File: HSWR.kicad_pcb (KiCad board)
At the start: 4 copper layers, 152 x 139 mm, 159 parts, among them IC1 B1212S-2W, IC3 JW5052C, IC4 ADM3054, IC5 ADuM4160, J1 USB_B, J2 IO, J3 B+, J4 B-, J5 U, J6 V, J7 W, J8 SWD, J9 AVR-ISP-6, Q1 IXFK300N20X3, Q2 IXFK300N20X3, Q3 IXFK300N20X3, Q4 IXFK300N20X3, Q5 IXFK300N20X3, Q6 IXFK300N20X3, Q7 Q_NMOS_GDS, U1 ACS781xLRTR-150B, U10 AM26LV32xD, U11 ADuM120N1, U12 ADuM120N1, U13 PC355, U2 ACS781xLRTR-150B, U3 ACS781xLRTR-150B, U4 STM32F405RGTx, U5 IRS2186, U6 IRS2186, U7 IRS2186, U8 AP1117-50, U9 ATtiny13A-SU, Y1 8MHz

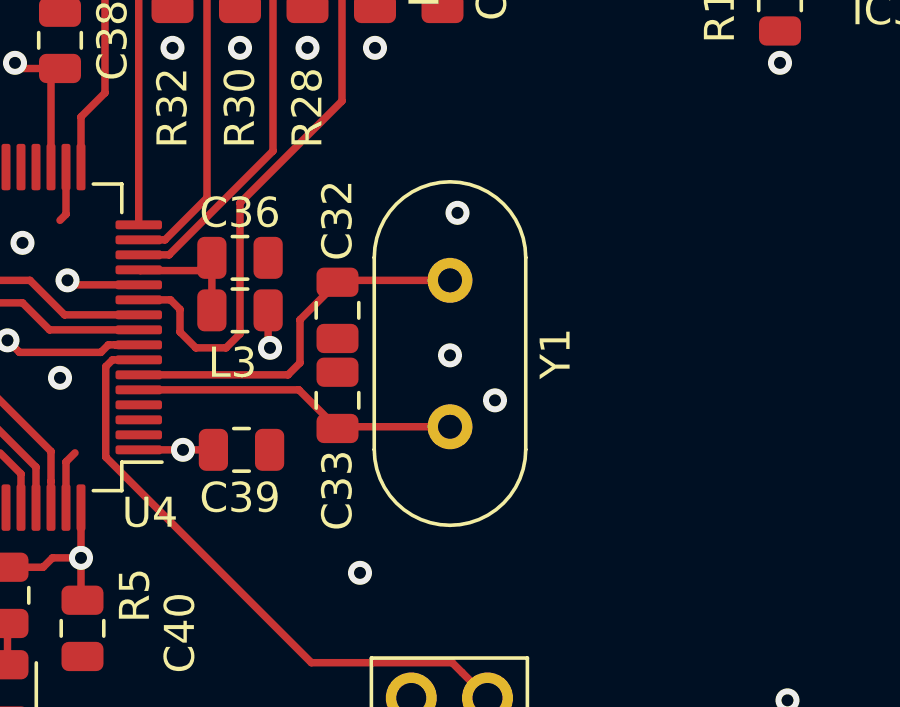
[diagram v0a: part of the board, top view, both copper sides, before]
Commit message: - upgraded project to KiCAD 7 - cleaned project - changed hall pullups to 10k
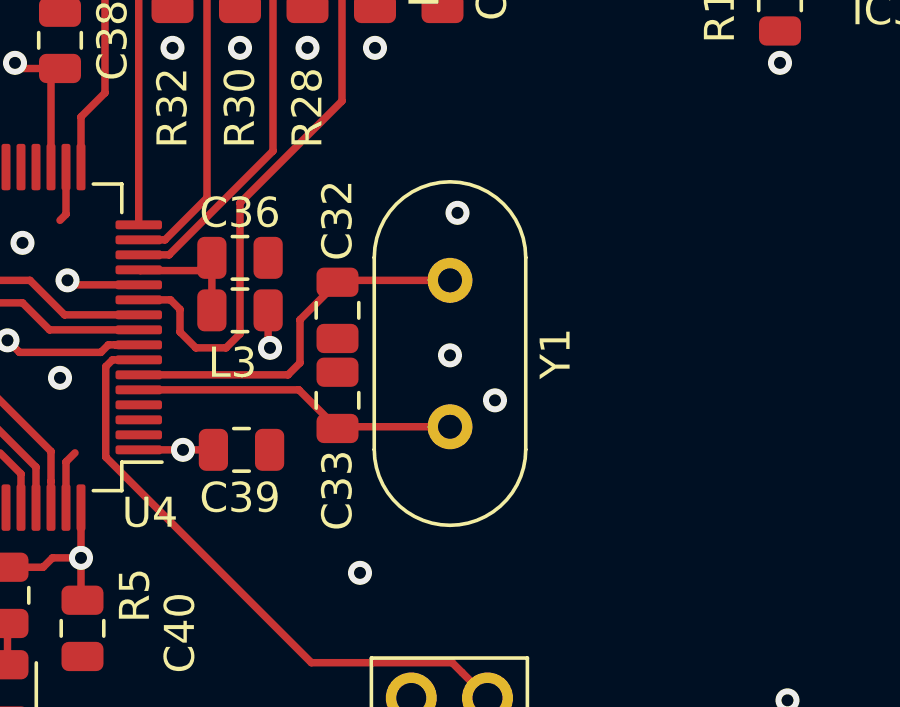
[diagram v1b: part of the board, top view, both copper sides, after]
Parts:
- R18, R19, R21, R22, R24, R25: value 1R -> 4R7
- R38, R39, R47: value 1k -> 10k
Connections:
- net /MCU/CAN_VSS_SENSE renamed /CAN bus transceiver/V+Sense
- net /USB/Device_D+ renamed /MCU/USB_DP
- net /USB/Device_D- renamed /MCU/USB_DM
- net /iso IO/UART renamed /MCU/UART_RX
- IC4 pad 10: (no net) -> unconnected-(IC4-VREF-Pad10)
- J8 pad 6: (no net) -> unconnected-(J8-Pin_6-Pad6)
- U1 pad 4: (no net) -> unconnected-(U1-NC-Pad4)
- U1 pad 7: (no net) -> unconnected-(U1-NC-Pad7)
- U10 pad 4: (no net) -> unconnected-(U10-G-Pad4)
- U2 pad 4: (no net) -> unconnected-(U2-NC-Pad4)
- U2 pad 7: (no net) -> unconnected-(U2-NC-Pad7)
- U3 pad 4: (no net) -> unconnected-(U3-NC-Pad4)
- U3 pad 7: (no net) -> unconnected-(U3-NC-Pad7)
- U4 pad 2: (no net) -> unconnected-(U4-PC13-Pad2)
- U4 pad 20: (no net) -> unconnected-(U4-PA4-Pad20)
- U4 pad 21: (no net) -> unconnected-(U4-PA5-Pad21)
- U4 pad 22: (no net) -> unconnected-(U4-PA6-Pad22)
- U4 pad 23: (no net) -> unconnected-(U4-PA7-Pad23)
- U4 pad 24: (no net) -> unconnected-(U4-PC4-Pad24)
- U4 pad 25: (no net) -> unconnected-(U4-PC5-Pad25)
- U4 pad 26: (no net) -> unconnected-(U4-PB0-Pad26)
- U4 pad 27: (no net) -> unconnected-(U4-PB1-Pad27)
- U4 pad 28: (no net) -> unconnected-(U4-PB2-Pad28)
- U4 pad 3: (no net) -> unconnected-(U4-PC14-Pad3)
- U4 pad 33: (no net) -> unconnected-(U4-PB12-Pad33)
- U4 pad 4: (no net) -> unconnected-(U4-PC15-Pad4)
- U4 pad 40: (no net) -> unconnected-(U4-PC9-Pad40)
- U4 pad 53: (no net) -> unconnected-(U4-PC12-Pad53)
- U4 pad 54: (no net) -> unconnected-(U4-PD2-Pad54)
- U4 pad 55: (no net) -> unconnected-(U4-PB3-Pad55)
- U4 pad 56: (no net) -> unconnected-(U4-PB4-Pad56)
- U4 pad 57: (no net) -> unconnected-(U4-PB5-Pad57)
- U4 pad 58: (no net) -> unconnected-(U4-PB6-Pad58)
- U4 pad 59: (no net) -> unconnected-(U4-PB7-Pad59)
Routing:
- added copper zone on In1.Cu, net +12VA
- added copper zone on In2.Cu, net +3V3
- added copper zone on In2.Cu, net +5VA
- added copper zone on In1.Cu, net /Mosfet driver/U_VP
- added copper zone on In2.Cu, net /Mosfet driver/U_VP
- added copper zone on In1.Cu, net /Mosfet driver/V_VP
- added copper zone on In2.Cu, net /Mosfet driver/V_VP
- added copper zone on In1.Cu, net /Mosfet driver/W_VP
- added copper zone on In2.Cu, net /Mosfet driver/W_VP
- added copper zone on In1.Cu, net GND
- removed copper zone on GND, net +12VA
- removed copper zone on Power1, net +3V3
- removed copper zone on Power1, net +5VA
- removed copper zone on GND, net /Mosfet driver/U_VP
- removed copper zone on Power1, net /Mosfet driver/U_VP
- removed copper zone on GND, net /Mosfet driver/V_VP
- removed copper zone on Power1, net /Mosfet driver/V_VP
- removed copper zone on GND, net /Mosfet driver/W_VP
- removed copper zone on Power1, net /Mosfet driver/W_VP
- removed copper zone on GND, net GND
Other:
- net class Default removed
- net class iso removed

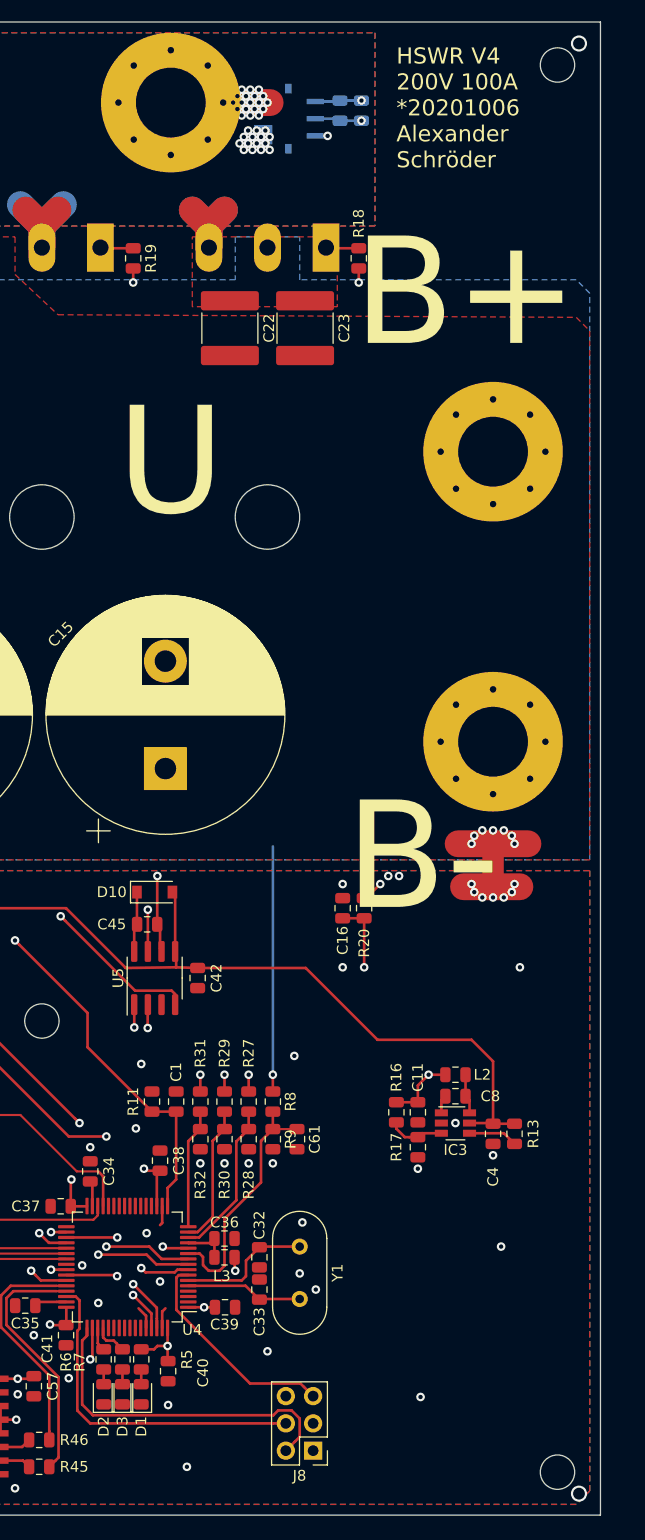
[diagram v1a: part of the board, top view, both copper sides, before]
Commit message: HSWR V4.1: - added opamp for better voltage measurement
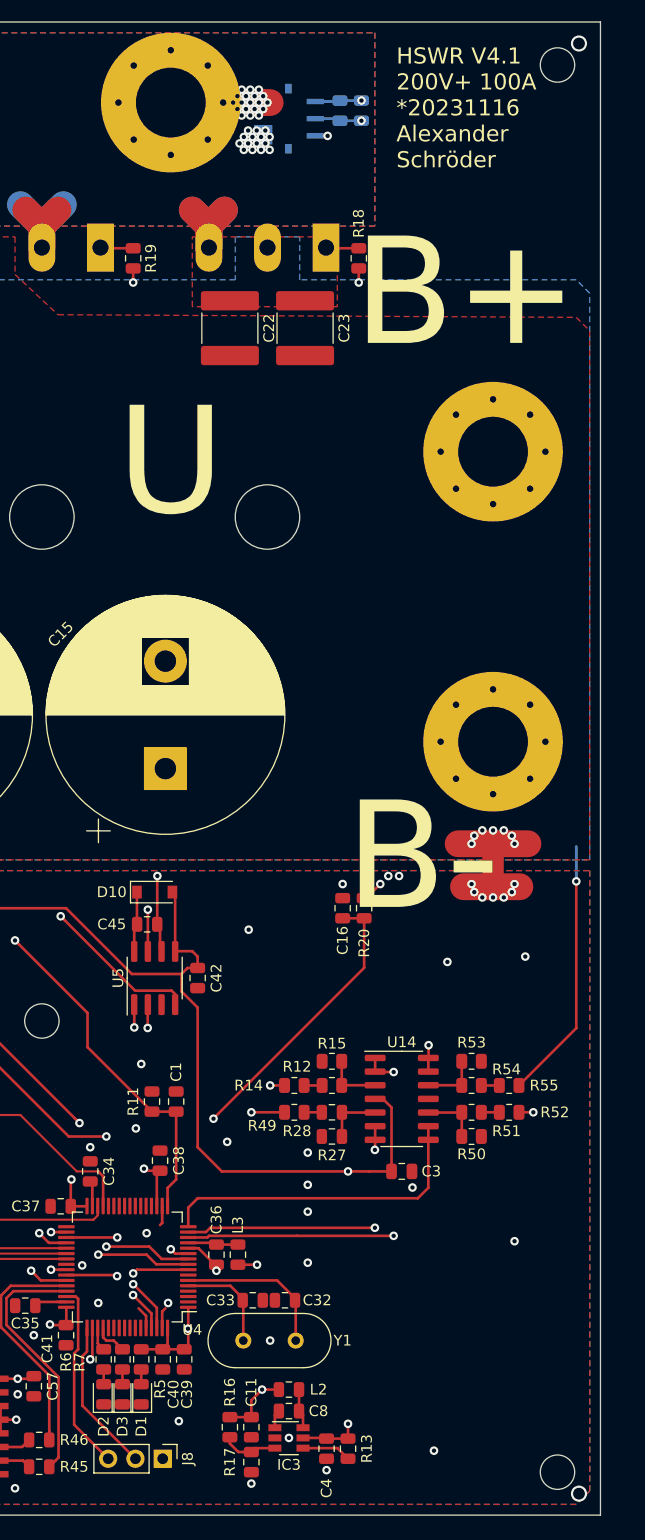
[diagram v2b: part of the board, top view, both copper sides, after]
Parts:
- removed C61: 1u, Capacitor_SMD:C_0805_2012Metric
- removed R29, R31, R8: 300k 0.1%, Resistor_SMD:R_0805_2012Metric
- removed R30, R32, R9: 4k7 0.1%, Resistor_SMD:R_0805_2012Metric
- added C3: 1u, Capacitor_SMD:C_0805_2012Metric, F.Cu at (200.5, 131.0)
- added R12: 150k, Resistor_SMD:R_0805_2012Metric, F.Cu at (194.0, 123.0)
- added R14: 150k, Resistor_SMD:R_0805_2012Metric, F.Cu at (190.5, 123.0)
- added R15: 4k7, Resistor_SMD:R_0805_2012Metric, F.Cu at (194.0, 120.8)
- added R49: 150k, Resistor_SMD:R_0805_2012Metric, F.Cu at (190.5, 125.5)
- added R50: 4k7, Resistor_SMD:R_0805_2012Metric, F.Cu at (207.0, 127.8)
- added R51: 150k, Resistor_SMD:R_0805_2012Metric, F.Cu at (207.0, 125.5)
- added R52: 150k, Resistor_SMD:R_0805_2012Metric, F.Cu at (210.5, 125.5)
- added R53: 4k7, Resistor_SMD:R_0805_2012Metric, F.Cu at (207.0, 120.8)
- added R54: 150k, Resistor_SMD:R_0805_2012Metric, F.Cu at (207.0, 123.0)
- added R55: 150k, Resistor_SMD:R_0805_2012Metric, F.Cu at (210.5, 123.0)
- added U14: Opamp_Quad, Package_SO:SO-14_3.9x8.65mm_P1.27mm, F.Cu at (200.5, 124.2)
- J8: value SWD -> ISP; footprint Connector_PinHeader_2.54mm:PinHeader_2x03_P2.54mm_Vertical -> Connector_PinHeader_2.54mm:PinHeader_1x03_P2.54mm_Vertical
- R27: value 300k 0.1% -> 4k7
- R28: value 4k7 0.1% -> 150k
- moved C11 33.2 mm to (186.5, 154.8)
- moved C4 33.2 mm to (193.5, 156.8)
- moved C8 33.2 mm to (190.0, 153.3)
- moved IC3 33.2 mm to (190.0, 155.8)
- moved L2 33.2 mm to (190.0, 151.3)
- moved R13 33.2 mm to (195.5, 156.8)
- moved R16 33.2 mm to (184.5, 154.8)
- moved R17 33.2 mm to (186.5, 158.1)
- moved J8 14.0 mm to (178.2, 157.8), turned to -90 degrees
- moved Y1 8.76 mm to (190.6, 146.8), turned to 180 degrees
- moved R27 8.40 mm to (194.0, 127.8), turned to 0 degrees
- moved R28 8.14 mm to (194.0, 125.5), turned to 180 degrees
- moved C39 6.16 mm to (180.2, 148.5), turned to -90 degrees
- moved C32 4.65 mm to (189.6, 143.0), turned to 0 degrees
- moved C36 1.68 mm to (183.2, 138.8), turned to 90 degrees
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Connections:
- J8 pad 1: +3V3 -> GND
- J8 pad 3: GND -> SWDIO
- R27 pad 1: /Mosfet driver/U_VP -> GND
- R27 pad 2: /MCU/U_U -> Net-(U14B-+)
- R28 pad 1: /MCU/U_U -> Net-(U14B-+)
- R28 pad 2: GND -> Net-(R28-Pad2)
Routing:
- net /Mosfet driver/W_VP: track 191.6 -> 236.2 mm
- net +12V: track 203.0 -> 236.7 mm, vias 1 -> 3
- net /MCU/U_U: track 14.6 -> 37.4 mm, vias 0 -> 2
- net NRST: track 20.3 -> 0.00 mm
- net /MCU/W_U: track 11.2 -> 30.6 mm
- net SWCLK: track 32.0 -> 14.4 mm
- net SWDIO: track 31.6 -> 17.6 mm
- net /MCU/V_U: track 13.1 -> 27.0 mm, vias 0 -> 2
- net /CAN bus transceiver/CAN_RX: track 68.9 -> 55.2 mm
- net /MCU/BUS_U: track 23.1 -> 36.1 mm, vias 0 -> 2
- net /Mosfet driver/V_VP: track 162.2 -> 168.3 mm
- net Net-(U14D-+): track 0.00 -> 5.37 mm
- net Net-(U14C-+): track 0.00 -> 5.37 mm
- net Net-(U14A-+): track 0.00 -> 5.37 mm
- net Net-(U14B-+): track 0.00 -> 5.18 mm
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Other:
- board text added: "HSWR V4.1 200V+ 100A *20231116 Alexander Schröder"
- board text removed: "HSWR V4 200V 100A *20201006 Alexander Schröder"

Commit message: - some layout work
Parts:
- removed the C29 at (110.8, 32.2)
- removed the C30 at (112.8, 32.2)
- removed the C31 at (114.8, 106.8)
- removed C51: 100n, Capacitor_SMD:C_0805_2012Metric
- removed JP1: H1, Jumper:SolderJumper-2_P1.3mm_Open_TrianglePad1.0x1.5mm
- removed JP3: H2, Jumper:SolderJumper-2_P1.3mm_Open_TrianglePad1.0x1.5mm
- removed JP4: H3, Jumper:SolderJumper-2_P1.3mm_Open_TrianglePad1.0x1.5mm
- removed JP5: EN, Jumper:SolderJumper-3_P2.0mm_Open_TrianglePad1.0x1.5mm
- removed NT1: Net-Tie_2, NetTie:NetTie-2_SMD_Pad2.0mm
- removed the R26 at (112.8, 106.8)
- removed the R38 at (103.8, 137.0)
- removed the R39 at (101.5, 138.2)
- removed the R47 at (103.8, 130.0)
- removed the U3 at (106.0, 33.0)
- added C10: 100n, Capacitor_SMD:C_0805_2012Metric, F.Cu at (183.0, 235.1)
- added C13: 10n, Capacitor_SMD:C_0805_2012Metric, F.Cu at (45.5, 108.5)
- added C60: 1u, Capacitor_SMD:C_0805_2012Metric, F.Cu at (174.5, 197.6)
- added C61: 1u, Capacitor_SMD:C_0805_2012Metric, F.Cu at (174.5, 200.7)
- added C62: 1u, Capacitor_SMD:C_0805_2012Metric, F.Cu at (174.5, 203.7)
- added C63: 1u, Capacitor_SMD:C_0805_2012Metric, F.Cu at (174.5, 206.7)
- added C64: 1u, Capacitor_SMD:C_0805_2012Metric, F.Cu at (174.5, 209.7)
- added C65: 1u, Capacitor_SMD:C_0805_2012Metric, F.Cu at (174.5, 212.7)
- added C66: 1u, Capacitor_SMD:C_0805_2012Metric, F.Cu at (174.5, 215.7)
- added C67: 100n, Capacitor_SMD:C_0805_2012Metric, F.Cu at (48.8, 240.4)
- added C68: 1u, Capacitor_SMD:C_0805_2012Metric, F.Cu at (48.8, 243.4)
- added C69: 330u 250V, Capacitor_THT:CP_Radial_D22.0mm_P10.00mm_SnapIn, F.Cu at (126.8, 163.5)
- added C70: 330u 250V, Capacitor_THT:CP_Radial_D22.0mm_P10.00mm_SnapIn, F.Cu at (103.2, 163.5)
- added C71: 4n7, Capacitor_SMD:C_0805_2012Metric, F.Cu at (48.8, 246.4)
- added C72: 330u 250V, Capacitor_THT:CP_Radial_D22.0mm_P10.00mm_SnapIn, F.Cu at (79.8, 163.5)
- added C73: 330u 250V, Capacitor_THT:CP_Radial_D22.0mm_P10.00mm_SnapIn, F.Cu at (56.2, 163.5)
- added C74: 330u 250V, Capacitor_THT:CP_Radial_D22.0mm_P10.00mm_SnapIn, F.Cu at (32.8, 163.5)
- added C75: 2u2 250V, Capacitor_SMD:C_2220_5750Metric, F.Cu at (34.8, 205.0)
- added C76: 2u2 250V, Capacitor_SMD:C_2220_5750Metric, F.Cu at (27.8, 205.0)
- added C77: 2u2 250V, Capacitor_SMD:C_2220_5750Metric, F.Cu at (70.0, 205.0)
- added C78: 2u2 250V, Capacitor_SMD:C_2220_5750Metric, F.Cu at (77.0, 205.0)
- added C79: 2u2 250V, Capacitor_SMD:C_2220_5750Metric, F.Cu at (111.8, 205.0)
- added C80: 2u2 250V, Capacitor_SMD:C_2220_5750Metric, F.Cu at (118.8, 205.0)
- added C81: 100n, Capacitor_SMD:C_0805_2012Metric, F.Cu at (53.3, 240.4)
- added C82: 1u, Capacitor_SMD:C_0805_2012Metric, F.Cu at (53.3, 243.4)
- added C83: 4n7, Capacitor_SMD:C_0805_2012Metric, F.Cu at (53.3, 246.4)
- added D10: RFN2L4S, Diode_SMD:D_SOD-123, F.Cu at (196.6, 213.4)
- added D8: RFN2L4S, Diode_SMD:D_SOD-123, F.Cu at (196.6, 206.7)
- added D9: RFN2L4S, Diode_SMD:D_SOD-123, F.Cu at (196.6, 210.0)
- added J10: W2, MountingHole:MountingHole_6.5mm_Pad_Via, F.Cu at (43.2, 225.5)
- added J13: CAN, Connector_Phoenix_MC:PhoenixContact_MCV_1,5_4-G-3.5_1x04_P3.50mm_Vertical, F.Cu at (19.0, 141.5)
- added J14: Motor1, Connector_Phoenix_MC:PhoenixContact_MCV_1,5_6-G-3.5_1x06_P3.50mm_Vertical, F.Cu at (19.0, 93.5)
- added J15: FAN, Connector_Phoenix_MC:PhoenixContact_MCV_1,5_2-G-3.5_1x02_P3.50mm_Vertical, F.Cu at (34.8, 115.2)
- added J8: U2, MountingHole:MountingHole_6.5mm_Pad_Via, F.Cu at (127.2, 225.5)
- added J9: V2, MountingHole:MountingHole_6.5mm_Pad_Via, F.Cu at (85.2, 225.5)
- added Q10: IXFK300N20X3, HSWR:TO-264-3_Horizontal_TabUp_6mm_hole, B.Cu at (68.0, 212.0)
- added Q11: IXFK300N20X3, HSWR:TO-264-3_Horizontal_TabUp_6mm_hole, B.Cu at (88.8, 212.0)
- added Q12: IXFK300N20X3, HSWR:TO-264-3_Horizontal_TabUp_6mm_hole, B.Cu at (25.8, 212.0)
- added Q13: IXFK300N20X3, HSWR:TO-264-3_Horizontal_TabUp_6mm_hole, B.Cu at (46.8, 212.0)
- added Q8: IXFK300N20X3, HSWR:TO-264-3_Horizontal_TabUp_6mm_hole, B.Cu at (109.8, 212.0)
- added Q9: IXFK300N20X3, HSWR:TO-264-3_Horizontal_TabUp_6mm_hole, B.Cu at (130.8, 212.0)
- added R18: 100R, Resistor_SMD:R_0805_2012Metric, F.Cu at (41.5, 108.5)
- added R19: 1k, Resistor_SMD:R_0805_2012Metric, F.Cu at (43.5, 108.5)
- added R20: 10k, Resistor_SMD:R_0805_2012Metric, F.Cu at (39.5, 108.5)
- added R50: 4k7, Resistor_SMD:R_0805_2012Metric, F.Cu at (187.4, 197.6)
- added R51: 4k7, Resistor_SMD:R_0805_2012Metric, F.Cu at (187.4, 200.6)
- added R52: 4k7, Resistor_SMD:R_0805_2012Metric, F.Cu at (187.4, 203.5)
- added R53: 150k, Resistor_SMD:R_0805_2012Metric, F.Cu at (191.8, 197.6)
- added R54: 150k, Resistor_SMD:R_0805_2012Metric, F.Cu at (191.8, 200.6)
- added R55: 150k, Resistor_SMD:R_0805_2012Metric, F.Cu at (191.8, 203.5)
- added R56: 150k, Resistor_SMD:R_0805_2012Metric, F.Cu at (196.2, 197.6)
- added R57: 150k, Resistor_SMD:R_0805_2012Metric, F.Cu at (196.2, 200.6)
- added R58: 150k, Resistor_SMD:R_0805_2012Metric, F.Cu at (196.2, 203.5)
- added R59: 4R7, Resistor_SMD:R_0805_2012Metric, F.Cu at (106.8, 211.2)
- added R60: 4R7, Resistor_SMD:R_0805_2012Metric, F.Cu at (127.8, 211.2)
- added R61: 1k, Resistor_SMD:R_0805_2012Metric, F.Cu at (62.2, 246.2)
- added R62: 4R7, Resistor_SMD:R_0805_2012Metric, F.Cu at (65.0, 211.2)
- added R63: 4R7, Resistor_SMD:R_0805_2012Metric, F.Cu at (85.8, 211.2)
- added R64: 1k, Resistor_SMD:R_0805_2012Metric, F.Cu at (66.6, 246.2)
- added R65: 4R7, Resistor_SMD:R_0805_2012Metric, F.Cu at (22.8, 211.2)
- added R66: 4R7, Resistor_SMD:R_0805_2012Metric, F.Cu at (43.8, 211.2)
- added RN1: 10k, Resistor_SMD:R_Array_Convex_4x0603, F.Cu at (29.0, 119.8)
- added RN2: 10k, Resistor_SMD:R_Array_Convex_4x0603, F.Cu at (26.5, 127.8)
- added U15: IRS2186, Package_SO:SOIC-8_3.9x4.9mm_P1.27mm, F.Cu at (181.2, 187.0)
- added U16: IRS2186, Package_SO:SOIC-8_3.9x4.9mm_P1.27mm, F.Cu at (181.0, 205.8)
- added U17: IRS2186, Package_SO:SOIC-8_3.9x4.9mm_P1.27mm, F.Cu at (181.0, 212.3)
- added U18: Opamp_Quad, Package_SO:SO-14_3.9x8.65mm_P1.27mm, F.Cu at (189.4, 210.1)
- added U19: ACS781xLRTR-150B, Sensor_Current:Allegro_PSOF-7_4.8x6.4mm_P1.60mm, F.Cu at (34.7, 246.6)
- added U20: ACS781xLRTR-150B, Sensor_Current:Allegro_PSOF-7_4.8x6.4mm_P1.60mm, F.Cu at (34.7, 254.6)
- added U5: ADuM120N, Package_SO:SOIC-8_3.9x4.9mm_P1.27mm, F.Cu at (48.0, 116.0)
- added U6: ADuM261N, Package_SO:SOIC-16W_7.5x12.8mm_P1.27mm, F.Cu at (48.0, 126.2)
- C41: renamed from C20; footprint Capacitor_SMD:C_2220_5650Metric -> Capacitor_SMD:C_2220_5750Metric
- C42: renamed from C21; footprint Capacitor_SMD:C_2220_5650Metric -> Capacitor_SMD:C_2220_5750Metric
- C43: renamed from C22; footprint Capacitor_SMD:C_2220_5650Metric -> Capacitor_SMD:C_2220_5750Metric
- C44: renamed from C23; footprint Capacitor_SMD:C_2220_5650Metric -> Capacitor_SMD:C_2220_5750Metric
- C45: renamed from C24; footprint Capacitor_SMD:C_2220_5650Metric -> Capacitor_SMD:C_2220_5750Metric
- C46: renamed from C25; footprint Capacitor_SMD:C_2220_5650Metric -> Capacitor_SMD:C_2220_5750Metric
- C49: value 100n -> 4n7
- C59: value 100n -> 22u/6V3
- J1: renamed from J2; value IO -> Motor1; footprint Connector_IDC:IDC-Header_2x08_P2.54mm_Vertical_Lock -> Connector_Phoenix_MC:PhoenixContact_MCV_1,5_6-G-3.5_1x06_P3.50mm_Vertical
- J5: value U -> U1
- J6: value V -> V1
- J7: value W -> W1
- R3: value 120R -> 470R
- R33, R34, R4: value 120R -> 150k
- R37: value 100R -> 150k
- U10: value AM26LV32xD -> IRS2186; footprint Package_SO:SOIC-16_3.9x9.9mm_P1.27mm -> Package_SO:SOIC-8_3.9x4.9mm_P1.27mm
- U11: value ADuM120N1 -> IRS2186
- U12: value ADuM120N1 -> ACS781xLRTR-150B; footprint Package_SO:SOIC-8_3.9x4.9mm_P1.27mm -> Sensor_Current:Allegro_PSOF-7_4.8x6.4mm_P1.60mm; moved to B.Cu
- U13: value PC355 -> ACS781xLRTR-150B; footprint Package_SO:SO-4_4.4x4.3mm_P2.54mm -> Sensor_Current:Allegro_PSOF-7_4.8x6.4mm_P1.60mm; moved to B.Cu
- U3: renamed from U9; footprint Package_SO:SOIJ-8_5.3x5.3mm_P1.27mm -> Package_SO:SO-8_5.3x6.2mm_P1.27mm
- moved U10 121.6 mm to (180.8, 223.3)
- moved U11 116.1 mm to (189.8, 223.8)
- moved U13 106.1 mm to (74.2, 224.0), turned to 0 degrees
- moved R3 102.1 mm to (178.8, 149.6)
- moved R33 102.1 mm to (178.8, 142.8)
- moved R34 102.1 mm to (178.8, 139.6)
- moved R4 102.1 mm to (178.8, 146.3)
- moved C49 101.8 mm to (95.5, 247.8)
- moved U12 92.7 mm to (116.5, 224.0)
- moved REF** 87.1 mm to (163.2, 229.0)
- moved REF** 87.1 mm to (19.2, 229.0)
- moved R27 69.8 mm to (35.8, 129.5)
- moved C6 69.2 mm to (34.8, 145.6)
- moved C12 68.1 mm to (41.5, 114.0), turned to 180 degrees
- moved Q1 67.3 mm to (29.2, 107.8), turned to 90 degrees
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- renumbered C60 to C11, C50 to C12, C58 to C14, C32 to C16, C33 to C17, C34 to C18, C35 to C19, C55 to C2, C36 to C20, C37 to C21, C38 to C22, C39 to C23, C40 to C24, C41 to C25, C42 to C26, C43 to C27, C44 to C28, C45 to C29, C56 to C3, C46 to C30, C47 to C31, C3 to C32, C12 to C33, C13 to C34, C14 to C35, C15 to C36, C16 to C37, C17 to C38, C18 to C39, C57 to C4, C19 to C40, C26 to C47, C27 to C48, C28 to C49, C52 to C5, C2 to C53, C4 to C54, C5 to C55, C6 to C56, C8 to C57, C9 to C58, C11 to C59, C53 to C6, C54 to C7, C62 to C8, C48 to C9, D4 to D1, D3 to D2, D2 to D3, D1 to D4, D10 to D5, D11 to D6, D12 to D7, IC5 to IC1, IC4 to IC2, IC1 to IC3, IC3 to IC4, J9 to J11, J8 to J12, J1 to J2, L3 to L1, Q7 to Q1, Q1 to Q2, Q2 to Q3, Q3 to Q4, Q4 to Q5, Q5 to Q6, Q6 to Q7, R7 to R1, R42 to R10, R43 to R11, R44 to R12, R45 to R13, R46 to R14, R40 to R15, R1 to R16, R2 to R17, R6 to R2, R35 to R22, R48 to R26, R36 to R27, R15 to R29, R5 to R3, R27 to R30, R50 to R31, R12 to R32, R28 to R33, R51 to R34, R14 to R35, R49 to R36, R52 to R37, R18 to R38, R19 to R39, R55 to R4, R20 to R40, R21 to R41, R22 to R42, R23 to R43, R24 to R44, R25 to R45, R13 to R47, R16 to R48, R17 to R49, R54 to R5, R53 to R6, R10 to R7, R11 to R8, R41 to R9, U14 to U1, U6 to U10, U7 to U11, U1 to U12, U2 to U13, U8 to U2, U4 to U8, U5 to U9
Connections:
- net /MCU/U_I renamed /MCU/U1_I
- net /MCU/U_PWM_H renamed /MCU/U1_PWM_H
- net /MCU/U_PWM_L renamed /MCU/U1_PWM_L
- net /MCU/U_U renamed /MCU/U1_U
- net /MCU/V_U renamed /MCU/V1_U
- net /MCU/W_U renamed /MCU/W1_U
- net /Mosfet driver/U_GH renamed /Mosfet driver 1/U_GH
- net /Mosfet driver/U_GL renamed /Mosfet driver 1/U_GL
- C29 pad 2: /Mosfet driver/U_VP -> /Mosfet driver 1/U_VP
- C30 pad 1: Net-(D11-K) -> Net-(D6-K)
- C30 pad 2: /Mosfet driver/V_VP -> /Mosfet driver 1/V_VP
- C31 pad 1: Net-(D12-K) -> Net-(D7-K)
- C31 pad 2: /Mosfet driver/W_VP -> /Mosfet driver 1/W_VP
- C49 pad 1: /MCU/V_I -> /Power MOSFETS 1/V_I
- C49 pad 1: +5VA -> /Power MOSFETS 1/V_I
- C49 pad 2: Earth -> GND
- C8 pad 1: /iso IO/M_Temp -> /iso IO/M1_Temp
- D4 pad 2: Net-(D1-A) -> Net-(D4-A)
- D6 pad 1: Net-(D11-K) -> Net-(D6-K)
- D7 pad 1: Net-(D12-K) -> Net-(D7-K)
- F1 pad 2: Net-(J2-Pin_1) -> Net-(J13-Pin_1)
- J1 pad 1: Net-(J2-Pin_1) -> +12VA
- J1 pad 2: /CAN bus transceiver/CANH -> /iso IO/Hall1_A
- J1 pad 3: /CAN bus transceiver/CANL -> /iso IO/Hall1_B
- J1 pad 4: Earth -> /iso IO/Hall1_C
- J1 pad 5: /iso IO/Hall_1A -> /iso IO/M1_Temp
- J1 pad 6: /iso IO/Hall_1B -> Earth
- J11 pad 1: Net-(J9-MISO) -> /iso IO/M2_Temp
- J5 pad 1: /Power MOSFETS/U -> /Power MOSFETS 1/U
- J6 pad 1: /Power MOSFETS/V -> /Power MOSFETS 1/V
- J7 pad 1: /Power MOSFETS/W -> /W_1
- Q1 pad 1: Net-(Q7-G) (its old number) -> Net-(Q1-G)
- Q2 pad 3: /Mosfet driver/U_VP -> /Mosfet driver 1/U_VP
- Q3 pad 2: /Mosfet driver/U_VP -> /Mosfet driver 1/U_VP
- Q4 pad 3: /Mosfet driver/V_VP -> /Mosfet driver 1/V_VP
- Q5 pad 2: /Mosfet driver/V_VP -> /Mosfet driver 1/V_VP
- Q6 pad 3: /Mosfet driver/W_VP -> /Mosfet driver 1/W_VP
- Q7 pad 2: /Mosfet driver/W_VP -> /Mosfet driver 1/W_VP
- R16 pad 2: /iso IO/M_Temp -> /iso IO/M1_Temp
- R17 pad 2: /iso IO/M_Temp -> /iso IO/M1_Temp
- R22 pad 2: /iso IO/M_Temp -> /iso IO/M1_Temp
- R27 pad 1: Net-(Q7-G) (its old number) -> Net-(Q1-G)
- R3 pad 1: Net-(D1-A) -> Net-(D4-A)
- R3 pad 1: /iso IO/Hall_1B -> Net-(D4-A)
- R3 pad 2: /iso IO/Hall_1A -> +3V3
- R30 pad 2: Net-(U14B-+) -> Net-(U1B-+)
- R31 pad 2: Net-(U14C-+) -> Net-(U1C-+)
- R33 pad 1: Net-(U14B-+) -> Net-(U1B-+)
- R33 pad 2: Net-(R28-Pad2) -> Net-(R33-Pad2)
- R33 pad 1: /iso IO/Hall_3B -> Net-(U1B-+)
- R33 pad 2: /iso IO/Hall_3A -> Net-(R33-Pad2)
- R34 pad 1: /iso IO/UART_B -> Net-(U1C-+)
- R34 pad 2: /iso IO/UART_A -> Net-(R34-Pad2)
- R34 pad 1: Net-(U14C-+) -> Net-(U1C-+)
- R34 pad 2: Net-(R51-Pad2) -> Net-(R34-Pad2)
- R35 pad 2: /Mosfet driver/U_VP -> /Mosfet driver 1/U_VP
- R36 pad 1: Net-(R28-Pad2) -> Net-(R33-Pad2)
- R36 pad 2: /Mosfet driver/V_VP -> /Mosfet driver 1/V_VP
- R37 pad 1: /MCU/Fan_CPU -> Net-(R34-Pad2)
- R37 pad 2: Net-(R37-Pad2) -> /Mosfet driver 1/W_VP
- R37 pad 1: Net-(R51-Pad2) -> Net-(R34-Pad2)
- R37 pad 2: /Mosfet driver/W_VP -> /Mosfet driver 1/W_VP
- R4 pad 1: /iso IO/Hall_2B -> Net-(R4-Pad1)
- R4 pad 2: /iso IO/Hall_2A -> +BATT
- R4 pad 1: Net-(R54-Pad2) -> Net-(R4-Pad1)
- R40 pad 2: Net-(U1-VOUT) -> Net-(U12-VOUT)
- R41 pad 2: /Mosfet driver/V_GH -> /Mosfet driver 1/V_GH
- R42 pad 2: /Mosfet driver/V_GL -> /Mosfet driver 1/V_GL
- R43 pad 1: /MCU/V_I -> /Power MOSFETS 1/V_I
- R43 pad 2: Net-(U2-VOUT) -> Net-(U13-VOUT)
- R44 pad 2: /Mosfet driver/W_GH -> /Mosfet driver 1/W_GH
- R45 pad 2: /Mosfet driver/W_GL -> /Mosfet driver 1/W_GL
- R5 pad 2: Net-(R54-Pad2) -> Net-(R4-Pad1)
- U1 pad 10: Net-(U14C-+) -> Net-(U1C-+)
- U1 pad 5: Net-(U14B-+) -> Net-(U1B-+)
- U10 pad 1: /MCU/V_PWM_H -> /MCU/V1_PWM_H
- U10 pad 2: /MCU/V_PWM_L -> /MCU/V1_PWM_L
- U10 pad 4: /Mosfet driver/V_GL -> /Mosfet driver 1/V_GL
- U10 pad 6: /Mosfet driver/V_VP -> /Mosfet driver 1/V_VP
- U10 pad 7: /Mosfet driver/V_GH -> /Mosfet driver 1/V_GH
- U10 pad 8: Net-(D11-K) -> Net-(D6-K)
- U10 pad 1: /iso IO/Hall_1B -> /MCU/V1_PWM_H
- U10 pad 2: /iso IO/Hall_1A -> /MCU/V1_PWM_L
- U10 pad 3: Net-(JP1-B) -> GND
- U10 pad 4: unconnected-(U10-G-Pad4) -> /Mosfet driver 1/V_GL
- U10 pad 5: Net-(JP3-B) -> +12V
- U10 pad 6: /iso IO/Hall_2A -> /Mosfet driver 1/V_VP
- U10 pad 7: /iso IO/Hall_2B -> /Mosfet driver 1/V_GH
- U10 pad 8: Earth -> Net-(D6-K)
- U11 pad 1: /MCU/W_PWM_H -> /MCU/W1_PWM_H
- U11 pad 2: /MCU/W_PWM_L -> /MCU/W1_PWM_L
- U11 pad 4: /Mosfet driver/W_GL -> /Mosfet driver 1/W_GL
- U11 pad 6: /Mosfet driver/W_VP -> /Mosfet driver 1/W_VP
- U11 pad 7: /Mosfet driver/W_GH -> /Mosfet driver 1/W_GH
- U11 pad 8: Net-(D12-K) -> Net-(D7-K)
- U11 pad 1: +5VA -> /MCU/W1_PWM_H
- U11 pad 2: Net-(JP1-B) -> /MCU/W1_PWM_L
- U11 pad 3: Net-(JP3-B) -> GND
- U11 pad 4: Earth -> /Mosfet driver 1/W_GL
- U11 pad 5: GND -> +12V
- U11 pad 6: /MCU/HALL_2 -> /Mosfet driver 1/W_VP
- U11 pad 7: /MCU/HALL_1 -> /Mosfet driver 1/W_GH
- U11 pad 8: +3V3 -> Net-(D7-K)
- U12 pad 1: +5VA -> +3V3
- U12 pad 2: Net-(JP4-B) -> GND
- U12 pad 3: Net-(J9-MISO) -> Net-(U12-VOUT)
- U12 pad 4: Earth -> unconnected-(U12-NC-Pad4)
- U12 pad 5: GND -> /Mosfet driver 1/U_VP
- U12 pad 6: /MCU/UART_RX -> /Power MOSFETS 1/U
- U12 pad 7: /MCU/HALL_3 -> unconnected-(U12-NC-Pad7)
- U12 pad 3: Net-(U1-VOUT) -> Net-(U12-VOUT)
- U12 pad 4: unconnected-(U1-NC-Pad4) -> unconnected-(U12-NC-Pad4)
- U12 pad 5: /Mosfet driver/U_VP -> /Mosfet driver 1/U_VP
- U12 pad 6: /Power MOSFETS/U -> /Power MOSFETS 1/U
- U12 pad 7: unconnected-(U1-NC-Pad7) -> unconnected-(U12-NC-Pad7)
- U13 pad 3: Net-(U2-VOUT) -> Net-(U13-VOUT)
- U13 pad 4: unconnected-(U2-NC-Pad4) -> unconnected-(U13-NC-Pad4)
- U13 pad 5: /Mosfet driver/V_VP -> /Mosfet driver 1/V_VP
- U13 pad 6: /Power MOSFETS/V -> /Power MOSFETS 1/V
- U13 pad 7: unconnected-(U2-NC-Pad7) -> unconnected-(U13-NC-Pad7)
- U13 pad 1: Net-(R37-Pad2) -> +3V3
- U13 pad 3: Net-(Q7-G) (its old number) -> Net-(U13-VOUT)
- U13 pad 4: +12VA -> unconnected-(U13-NC-Pad4)
- U2 pad 1: Earth -> +12VA
- U2 pad 2: +5VA -> Earth
- U2 pad 3: +12VA -> +5VA
- U3 pad 3: /iso IO/M_Temp -> /iso IO/M1_Temp
- U3 pad 6: Net-(J9-MISO) -> /iso IO/M2_Temp
- U8 pad 10: /MCU/W_I -> /MCU/U2_I
- U8 pad 11: /MCU/BUS_U -> /MCU/W2_I
- U8 pad 20: unconnected-(U4-PA4-Pad20) -> /MCU/U2_U
- U8 pad 21: unconnected-(U4-PA5-Pad21) -> /MCU/V2_U
- U8 pad 22: unconnected-(U4-PA6-Pad22) -> /MCU/W2_U
- U8 pad 23: unconnected-(U4-PA7-Pad23) -> /MCU/U2_PWM_L
- U8 pad 24: unconnected-(U4-PC4-Pad24) -> /MCU/BUS_U
- U8 pad 26: unconnected-(U4-PB0-Pad26) -> /MCU/V2_PWM_L
- U8 pad 27: unconnected-(U4-PB1-Pad27) -> /MCU/W2_PWM_L
- U8 pad 28: unconnected-(U4-PB2-Pad28) -> /MCU/H1_1
- U8 pad 35: /MCU/V_PWM_L -> /MCU/V1_PWM_L
- U8 pad 36: /MCU/W_PWM_L -> /MCU/W1_PWM_L
- U8 pad 37: /MCU/HALL_1 -> /MCU/U2_PWM_H
- U8 pad 38: /MCU/HALL_2 -> /MCU/V2_PWM_H
- U8 pad 39: /MCU/HALL_3 -> /MCU/W2_PWM_H
- U8 pad 42: /MCU/V_PWM_H -> /MCU/V1_PWM_H
- U8 pad 43: /MCU/W_PWM_H -> /MCU/W1_PWM_H
- U8 pad 55: unconnected-(U4-PB3-Pad55) -> /MCU/H1_2
- U8 pad 56: unconnected-(U4-PB4-Pad56) -> /MCU/H1_3
- U8 pad 57: unconnected-(U4-PB5-Pad57) -> /MCU/H2_1
- U8 pad 58: unconnected-(U4-PB6-Pad58) -> /MCU/H2_2
- U8 pad 59: unconnected-(U4-PB7-Pad59) -> /MCU/H2_3
- U8 pad 9: /MCU/V_I -> /MCU/W1_I
- U9 pad 6: /Mosfet driver/U_VP -> /Mosfet driver 1/U_VP
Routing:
- net +3V3: track 345.8 -> 14.1 mm, vias 19 -> 4
- net /Mosfet driver/W_VP: track 236.2 -> 0.00 mm, vias 17 -> 0
- net GND: track 243.8 -> 8.76 mm, vias 55 -> 4
- net +12V: track 236.7 -> 19.8 mm, vias 3 -> 0
- net /Mosfet driver/V_VP: track 168.3 -> 0.00 mm, vias 17 -> 0
- net /MCU/TEMP_INT: track 130.3 -> 1.34 mm, vias 2 -> 1
- net /Mosfet driver/U_VP: track 125.2 -> 0.00 mm, vias 17 -> 0
- net /MCU/W_PWM_H: track 89.0 -> 0.00 mm, vias 2 -> 0
- net /MCU/W_I: track 86.9 -> 0.00 mm, vias 2 -> 0
- net /MCU/W_PWM_L: track 84.8 -> 0.00 mm, vias 2 -> 0
- net /MCU/V_PWM_H: track 82.2 -> 0.00 mm, vias 2 -> 0
- net /Mosfet driver/V_GL: track 78.8 -> 0.00 mm, vias 2 -> 0
- net Net-(U1-VOUT): track 77.4 -> 0.00 mm, vias 2 -> 0
- net Net-(U3-VOUT): track 76.6 -> 0.00 mm, vias 2 -> 0
- net /Mosfet driver 1/U_GL: track 77.7 -> 1.31 mm, vias 2 -> 1
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- added copper zone on B.Cu, net /Mosfet driver 1/U_VP
- added copper zone on F.Cu, net /Mosfet driver 1/U_VP
- added copper zone on In1.Cu, net /Mosfet driver 1/U_VP
- added copper zone on In2.Cu, net /Mosfet driver 1/U_VP
- added copper zone on B.Cu, net /Mosfet driver 1/V_VP
- added copper zone on F.Cu, net /Mosfet driver 1/V_VP
- added copper zone on In1.Cu, net /Mosfet driver 1/V_VP
- added copper zone on In2.Cu, net /Mosfet driver 1/V_VP
- added copper zone on B.Cu, net /Mosfet driver 1/W_VP
- added copper zone on F.Cu, net /Mosfet driver 1/W_VP
- added copper zone on In1.Cu, net /Mosfet driver 1/W_VP
- added copper zone on In2.Cu, net /Mosfet driver 1/W_VP
- removed copper zone on B.Cu, net /Mosfet driver/U_VP
- removed copper zone on F.Cu, net /Mosfet driver/U_VP
- removed copper zone on In1.Cu, net /Mosfet driver/U_VP
- removed copper zone on In2.Cu, net /Mosfet driver/U_VP
- removed copper zone on B.Cu, net /Mosfet driver/V_VP
- removed copper zone on F.Cu, net /Mosfet driver/V_VP
- removed copper zone on In1.Cu, net /Mosfet driver/V_VP
- removed copper zone on In2.Cu, net /Mosfet driver/V_VP
- removed copper zone on B.Cu, net /Mosfet driver/W_VP
- removed copper zone on F.Cu, net /Mosfet driver/W_VP
- removed copper zone on In1.Cu, net /Mosfet driver/W_VP
- removed copper zone on In2.Cu, net /Mosfet driver/W_VP
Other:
- board size 152 x 139 mm -> 152 x 220 mm
